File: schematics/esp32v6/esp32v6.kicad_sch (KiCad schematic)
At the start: 2 parts

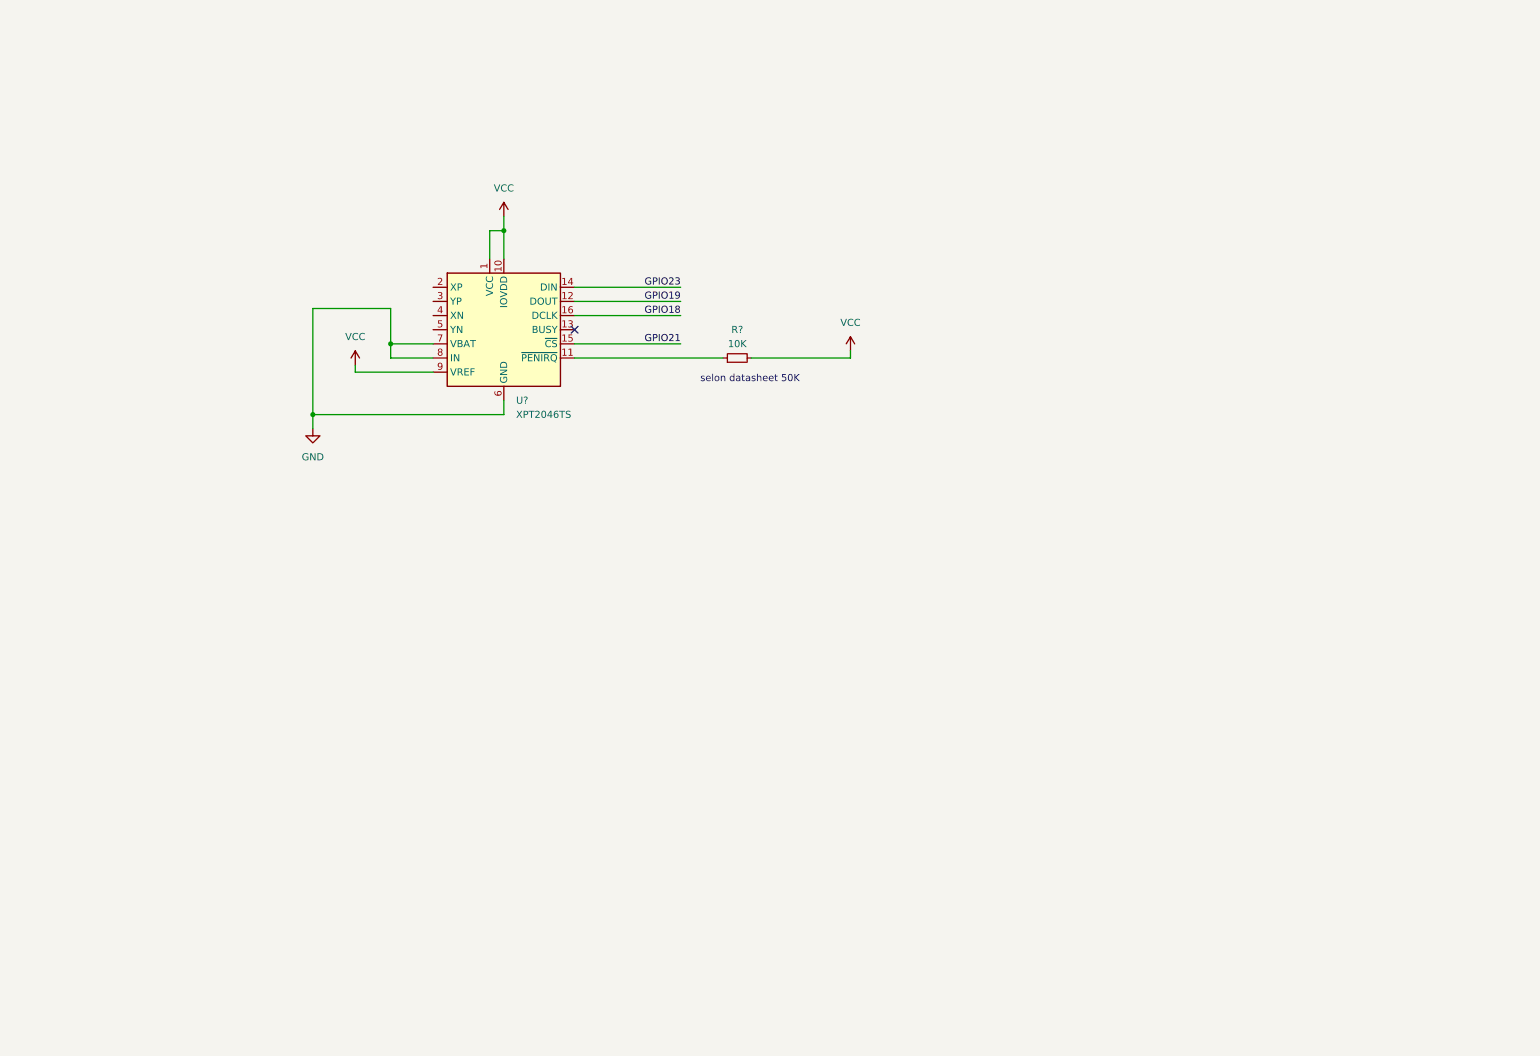
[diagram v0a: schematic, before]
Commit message: Reverse schematic for ESP32 done
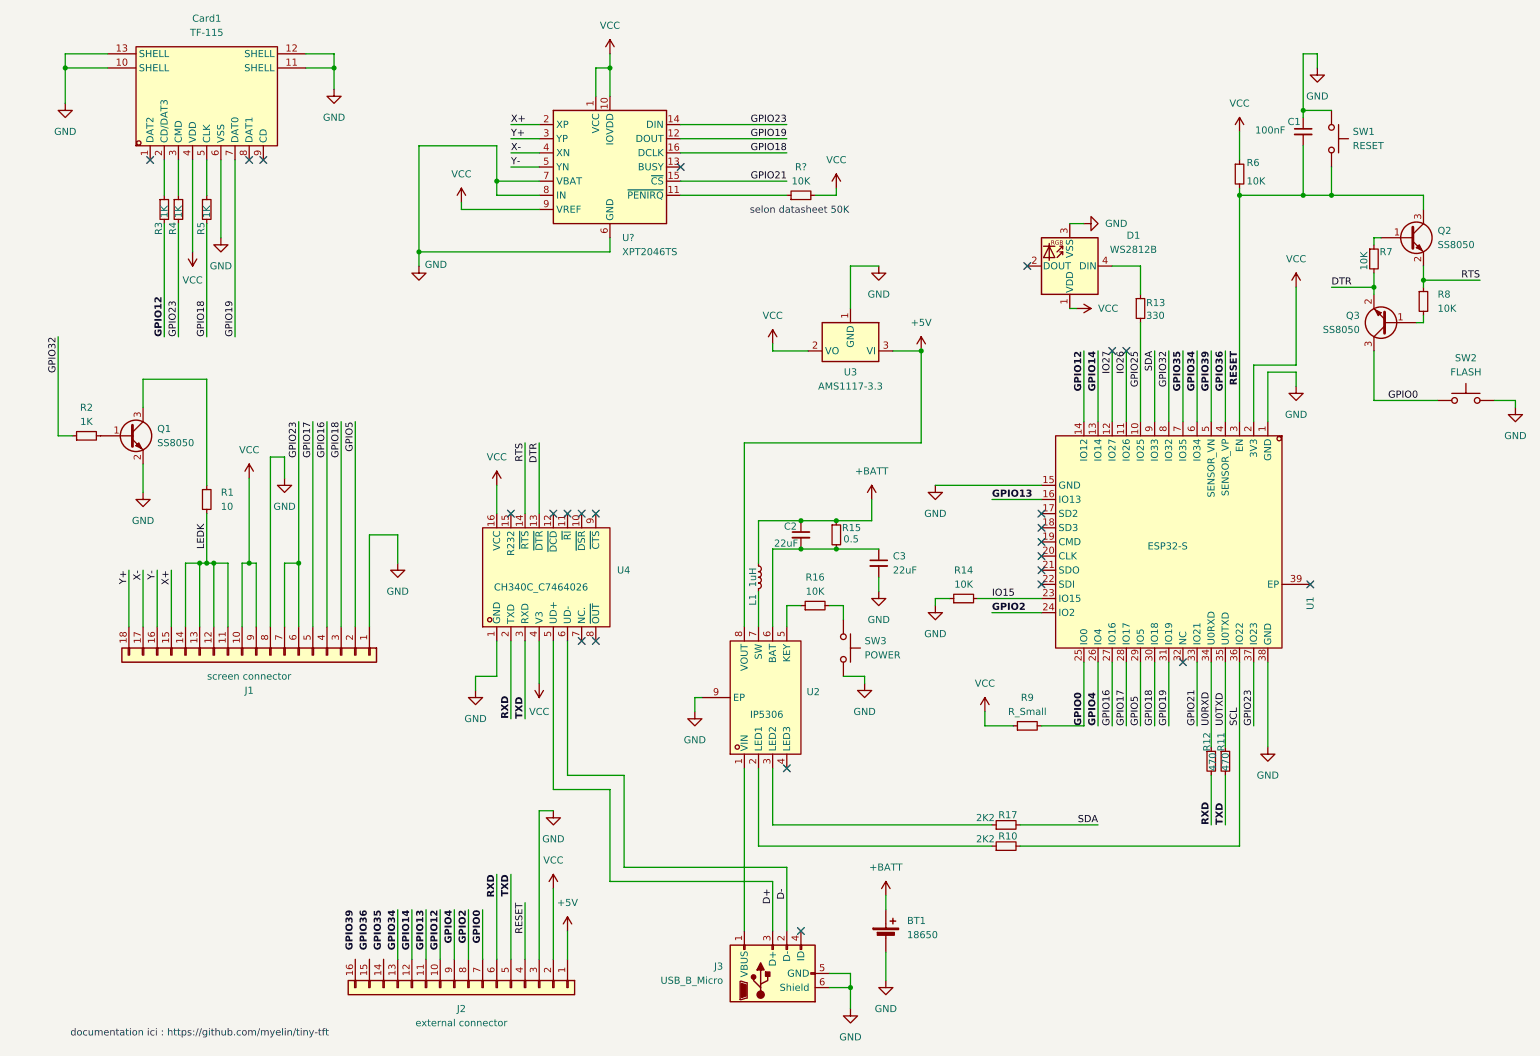
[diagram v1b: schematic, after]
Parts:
- added BT1: 18650, symbol Device:Battery_Cell
- added C1: 100nF, symbol Device:C_Small
- added C2, C3: 22uF, symbol Device:C_Small
- added Card1: TF-115, LSC_Symbols:TF-SMD_TF-115, symbol LSC_Symbols:TF-115
- added D1: WS2812B, LED_SMD:LED_WS2812B_PLCC4_5.0x5.0mm_P3.2mm, symbol LED:WS2812B
- added J1: screen connector, symbol Connector_Generic:Conn_01x18
- added J2: external connector, symbol Connector_Generic:Conn_01x16
- added J3: USB_B_Micro, symbol Connector:USB_B_Micro
- added L1: 1uH, symbol Device:L_Small
- added Q1, Q2, Q3: SS8050, Package_TO_SOT_SMD:SOT-23, symbol Transistor_BJT:SS8050
- added R1: 10, symbol Device:R_Small
- added R10, R17: 2K2, symbol Device:R_Small
- added R11, R12: 470, symbol Device:R_Small
- added R13: 330, symbol Device:R_Small
- added R14, R16, R6, R7, R8: 10K, symbol Device:R_Small
- added R15: 0.5, symbol Device:R_Small
- added R2, R3, R4, R5: 1K, symbol Device:R_Small
- added R9: R_Small, symbol Device:R_Small
- added SW1: RESET, symbol Switch:SW_Push
- added SW2: FLASH, symbol Switch:SW_Push
- added SW3: POWER, symbol Switch:SW_Push
- added U1: ESP32-S, LSC_Symbols:WIRELM-SMD_ESP32-S, symbol LSC_Symbols:ESP32-S
- added U2: IP5306, LSC_Symbols:ESOP-8_L4.9-W3.9-P1.27-LS6.0-BL-EP, symbol LSC_Symbols:IP5306
- added U3: AMS1117-3.3, Package_TO_SOT_SMD:SOT-223-3_TabPin2, symbol Regulator_Linear:AMS1117-3.3
- added U4: CH340C_C7464026, LSC_Symbols:SOP-16_L10.0-W3.9-P1.27-LS6.0-BL, symbol LSC_Symbols:CH340C_C7464026
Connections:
- net GND: now also BT1.2 (-), C1.1, C3.2, Card1.10 (SHELL), Card1.11 (SHELL), Card1.12 (SHELL), Card1.13 (SHELL), Card1.6 (VSS), D1.3 (VSS), J1.1 (Pin_1), J1.8 (Pin_8), J2.3 (Pin_3), J3.5 (GND), J3.6 (Shield), Q1.2 (E), R14.1, SW1.1, SW2.2, SW3.2, U1.1 (GND), U1.15 (GND), U1.38 (GND), U2.9 (EP), U3.1 (GND), U4.1 (GND)
- net GPIO18: now also J1.3 (Pin_3), R5.2, U1.30 (IO18)
- net GPIO19: now also Card1.7 (DAT0), U1.31 (IO19)
- net GPIO21: now also U1.33 (IO21)
- net GPIO23: now also J1.6 (Pin_6), J1.7 (Pin_7), R4.2, U1.37 (IO23)
- net VCC: now also Card1.4 (VDD), D1.1 (VDD), J1.10 (Pin_10), J1.9 (Pin_9), J2.2 (Pin_2), R6.1, R9.1, U1.2 (3V3), U3.2 (VO), U4.16 (VCC), U4.4 (V3)
- net X+: now reaches U?.2 (XP)
- net X+: now also J1.15 (Pin_15)
- net Y+: now reaches U?.3 (YP)
- net Y+: now also J1.18 (Pin_18)
- net X-: now reaches U?.4 (XN)
- net X-: now also J1.17 (Pin_17)
- net Y-: now reaches U?.5 (YN)
- net Y-: now also J1.16 (Pin_16)
- new net: R16.2, SW3.1
- new net: Q3.1 (B), R8.2
- new net: Q2.1 (B), R7.1
- new net: R16.1, U2.5 (KEY)
- new net: C2.2, C3.1, R15.2, U2.6 (BAT)
- new net: Q1.1 (B), R2.2
- new net: Card1.5 (CLK), R5.1
- new net: Card1.2 (CD/DAT3), R3.1
- new net: J3.1 (VBUS), U2.1 (VIN)
- new net: R17.1, U2.3 (LED2)
- new net: D1.4 (DIN), R13.1
- new net: L1.2, U2.7 (SW)
- new net: Card1.3 (CMD), R4.1
- new net: R10.1, U2.2 (LED1)
- new net: Q1.3 (C), R1.1
- new net +5V: J2.1 (Pin_1), U2.8 (VOUT), U3.3 (VI)
- new net +BATT: BT1.1 (+), C2.1, L1.1, R15.1
- new net D+: J3.3 (D+), U4.5 (UD+)
- new net D-: J3.2 (D-), U4.6 (UD-)
- new net DTR: Q3.2 (E), R7.2, U4.13 (~{DTR})
- new net GPIO0: J2.7 (Pin_7), Q3.3 (C), R9.2, SW2.1, U1.25 (IO0)
- new net GPIO12: J2.10 (Pin_10), R3.2, U1.14 (IO12)
- new net GPIO13: J2.11 (Pin_11), U1.16 (IO13)
- new net GPIO14: J2.12 (Pin_12), U1.13 (IO14)
- new net GPIO16: J1.4 (Pin_4), U1.27 (IO16)
- new net GPIO17: J1.5 (Pin_5), U1.28 (IO17)
- new net GPIO2: J2.8 (Pin_8), U1.24 (IO2)
- new net GPIO25: R13.2, U1.10 (IO25)
- new net GPIO32: R2.1, U1.8 (IO32)
- new net GPIO34: J2.13 (Pin_13), U1.6 (IO34)
- new net GPIO35: U1.7 (IO35)
- new net GPIO36: U1.4 (SENSOR_VP)
- new net GPIO39: U1.5 (SENSOR_VN)
- new net GPIO4: J2.9 (Pin_9), U1.26 (IO4)
- new net GPIO5: J1.2 (Pin_2), U1.29 (IO5)
- new net IO15: R14.2, U1.23 (IO15)
- new net IO26: U1.11 (IO26)
- new net IO27: U1.12 (IO27)
- new net LEDK: J1.11 (Pin_11), J1.12 (Pin_12), J1.13 (Pin_13), J1.14 (Pin_14), R1.2
- new net RESET: C1.2, J2.4 (Pin_4), Q2.3 (C), R6.2, SW1.2, U1.3 (EN)
- new net RTS: Q2.2 (E), R8.1, U4.14 (~{RTS})
- new net RXD: J2.6 (Pin_6), R12.2, U4.2 (TXD)
- new net SCL: R10.2, U1.36 (IO22)
- new net SDA: R17.2, U1.9 (IO33)
- new net TXD: J2.5 (Pin_5), R11.2, U4.3 (RXD)
- new net U0RXD: R12.1, U1.34 (U0RXD)
- new net U0TXD: R11.1, U1.35 (U0TXD)
- no-connect marks 1 -> 24
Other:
- note added: "documentation ici : https://github.com/myelin/tiny-tft"
- company: (none) -> LSC
- title: (none) -> ESP32Marauder
- moved on the sheet: R?, U?

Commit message: Updating schematic
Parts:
- removed U?: XPT2046TS, Package_SO:TSSOP-16_4.4x5mm_P0.65mm, symbol Driver_Display:XPT2046TS
- added U?: XPT2046, LSC_Symbols:TSSOP-16_L5.0-W4.4-P0.65-LS6.4-BL, symbol LSC_Symbols:XPT2046
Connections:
- net GND: now also U?.6 (GND), U?.7 (VBAT), U?.8 (AUX)
- net GPIO18: now also U?.16 (DCLK)
- net GPIO19: now also U?.12 (DOUT)
- net GPIO21: now also U?.15 (~{CS})
- net GPIO23: now also U?.14 (DIN)
- net VCC: now also U?.1 (VCC), U?.10 (IOVDD), U?.9 (VREF)
- net X+: now also U?.2 (XP)
- net X-: now also U?.4 (XN)
- net Y+: now also U?.3 (YP)
- net Y-: now also U?.5 (YN)
- net at R?.1: now also U?.11 (~{PENIRQ})
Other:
- moved on the sheet: R?
